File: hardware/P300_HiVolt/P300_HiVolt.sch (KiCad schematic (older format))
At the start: 10 parts, among them J1 Conn_01x02, J2 Conn_01x08, J3 Stiftleiste 6P - Molex, J4 Stiftleiste 6P - Molex, J5 12V, J6 5V, T1 HLK-PM12, T2 HLK-PM05

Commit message: Platinen V.23 in die Herstellung gegeben
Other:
- note added: "Pin3 (braun) Sommer"
- note added: "Pin4 (schwarz) Winter"
- moved on the sheet: J3, J4

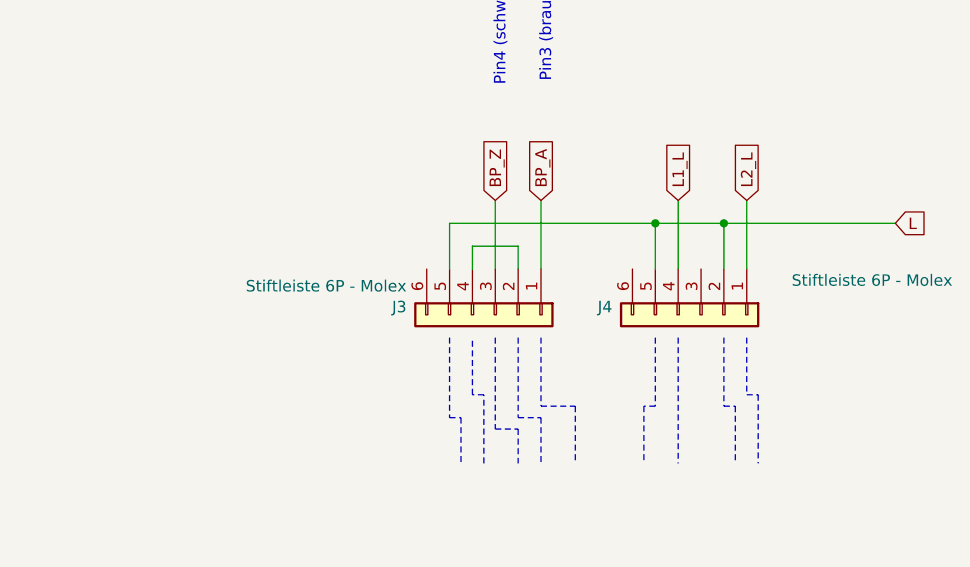
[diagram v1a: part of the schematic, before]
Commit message: Update  P300_HiVolt Platine
 - Anschluss zu Relais per Schraubklemmen, anstatt Molex Stecker, wegen der schwierigen Beschaffung und Crimpen der Molex Verbindung
 - Alternative für 5V Spannung Meanwell IRM-05-5 mit 5W(1A) Leistung hinzugefügt, empfohlen bei Verwendung Display
 - Platine 3mm verlängert
 - Bohr in Mitte/unten hinzugefügt
 - Leiterbahnen zu den Lüftern auf 2mm verbreitert
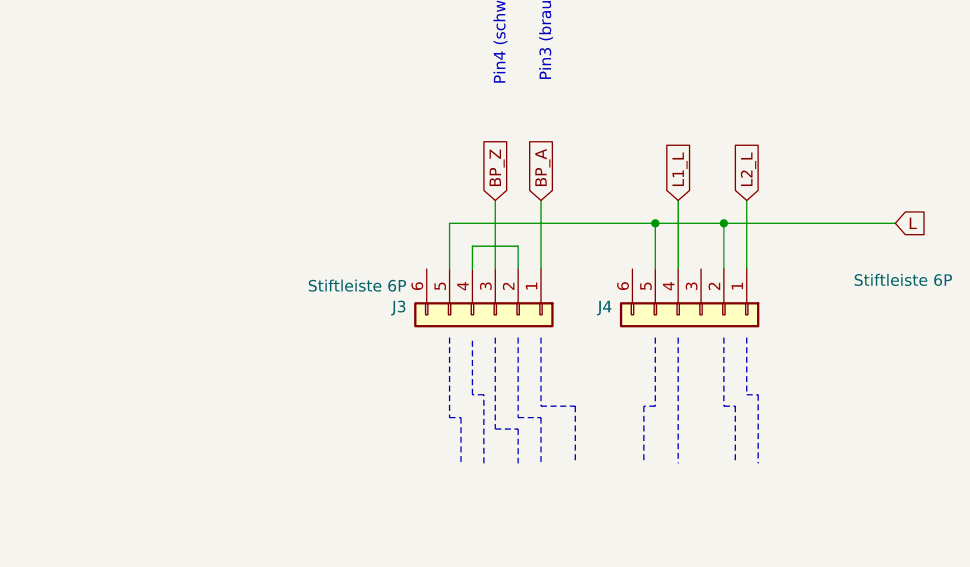
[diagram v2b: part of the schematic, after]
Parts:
- J3, J4: value Stiftleiste 6P - Molex -> Stiftleiste 6P; footprint Connectors_Molex:Molex_MiniFit-JR-5556-06A_2x03x4.20mm_Straight -> Connectors_Terminal_Blocks:TerminalBlock_bornier-6_P5.08mm
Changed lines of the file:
@@
 P 8200 2950
 F 0 "J3" V 8166 2562 50  0000 R CNN
-F 1 "Stiftleiste 6P - Molex" V 8075 2562 50  0000 R CNN
-F 2 "Connectors_Molex:Molex_MiniFit-JR-5556-06A_2x03x4.20mm_Straight" H 8200 2950 50  0001 C CNN
+F 1 "Stiftleiste 6P" V 8075 2562 50  0000 R CNN
+F 2 "Connectors_Terminal_Blocks:TerminalBlock_bornier-6_P5.08mm" H 8200 2950 50  0001 C CNN
 F 3 "~" H 8200 2950 50  0001 C CNN
 	1    8200 2950
@@
 P 9100 2950
 F 0 "J4" V 9066 2562 50  0000 R CNN
-F 1 "Stiftleiste 6P - Molex" V 8950 4050 50  0000 R CNN
-F 2 "Connectors_Molex:Molex_MiniFit-JR-5556-06A_2x03x4.20mm_Straight" H 9100 2950 50  0001 C CNN
+F 1 "Stiftleiste 6P" V 8950 4050 50  0000 R CNN
+F 2 "Connectors_Terminal_Blocks:TerminalBlock_bornier-6_P5.08mm" H 9100 2950 50  0001 C CNN
 F 3 "~" H 9100 2950 50  0001 C CNN
 	1    9100 2950
